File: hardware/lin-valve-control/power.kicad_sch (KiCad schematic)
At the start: 22 parts, among them U3 LTC3203BEDD-PBF, U4 BD9G341EFJ

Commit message: Uptdate title block
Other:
- company: (none) -> Gavin Hurlbut
- title: (none) -> LINBus Valve Controller
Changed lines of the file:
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@@
 (kicad_sch (version 20211123) (generator eeschema)
   (paper "A4")
+  (title_block
+    (title "LINBus Valve Controller")
+    (date "2023-02-17")
+    (rev "1.0")
+    (company "Gavin Hurlbut")
+  )
   (junction (at 109.347 133.096) (diameter 0) (color 0 0 0 0)
   )

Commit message: Add PCA9536 for the LINBus Address
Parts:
- renumbered U3 to U4, U4 to U5
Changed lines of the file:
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@@
   (symbol (lib_id "power:GND") (at 144.145 89.789 0) (unit 1)
     (in_bom yes) (on_board yes) (fields_autoplaced)
-    (property "Reference" "#PWR027" (id 0) (at 144.145 96.139 0)
+    (property "Reference" "#PWR030" (id 0) (at 144.145 96.139 0)
       (effects (font (size 1.27 1.27)) hide)
     )
@@
   (symbol (lib_id "power:+3V3") (at 100.457 116.967 0) (unit 1)
     (in_bom yes) (on_board yes) (fields_autoplaced)
-    (property "Reference" "#PWR021" (id 0) (at 100.457 120.777 0)
+    (property "Reference" "#PWR024" (id 0) (at 100.457 120.777 0)
       (effects (font (size 1.27 1.27)) hide)
     )
@@
   (symbol (lib_id "power:GND") (at 100.457 152.4 0) (unit 1)
     (in_bom yes) (on_board yes) (fields_autoplaced)
-    (property "Reference" "#PWR022" (id 0) (at 100.457 158.75 0)
+    (property "Reference" "#PWR025" (id 0) (at 100.457 158.75 0)
       (effects (font (size 1.27 1.27)) hide)
     )
@@
   (symbol (lib_id "power:GND") (at 197.358 58.674 0) (unit 1)
     (in_bom yes) (on_board yes) (fields_autoplaced)
-    (property "Reference" "#PWR033" (id 0) (at 197.358 65.024 0)
+    (property "Reference" "#PWR036" (id 0) (at 197.358 65.024 0)
       (effects (font (size 1.27 1.27)) hide)
     )
@@
   (symbol (lib_id "power:+3V3") (at 197.358 41.656 0) (unit 1)
     (in_bom yes) (on_board yes) (fields_autoplaced)
-    (property "Reference" "#PWR032" (id 0) (at 197.358 45.466 0)
+    (property "Reference" "#PWR035" (id 0) (at 197.358 45.466 0)
       (effects (font (size 1.27 1.27)) hide)
     )
@@
   (symbol (lib_id "power:GND") (at 149.098 56.515 0) (unit 1)
     (in_bom yes) (on_board yes) (fields_autoplaced)
-    (property "Reference" "#PWR028" (id 0) (at 149.098 62.865 0)
+    (property "Reference" "#PWR031" (id 0) (at 149.098 62.865 0)
       (effects (font (size 1.27 1.27)) hide)
     )
@@
   (symbol (lib_id "power:+BATT") (at 76.454 51.435 0) (unit 1)
     (in_bom yes) (on_board yes) (fields_autoplaced)
-    (property "Reference" "#PWR016" (id 0) (at 76.454 55.245 0)
+    (property "Reference" "#PWR019" (id 0) (at 76.454 55.245 0)
       (effects (font (size 1.27 1.27)) hide)
     )
@@
   (symbol (lib_id "Beirdo:BD9G341EFJ") (at 131.191 65.278 0) (unit 1)
     (in_bom yes) (on_board yes) (fields_autoplaced)
-    (property "Reference" "U4" (id 0) (at 133.2104 50.165 0)
+    (property "Reference" "U5" (id 0) (at 133.2104 50.165 0)
       (effects (font (size 1.27 1.27)) (justify left))
     )
@@
   (symbol (lib_id "power:GND") (at 89.027 150.114 0) (unit 1)
     (in_bom yes) (on_board yes) (fields_autoplaced)
-    (property "Reference" "#PWR018" (id 0) (at 89.027 156.464 0)
+    (property "Reference" "#PWR021" (id 0) (at 89.027 156.464 0)
       (effects (font (size 1.27 1.27)) hide)
     )
@@
   (symbol (lib_id "power:GND") (at 170.053 76.2 0) (unit 1)
     (in_bom yes) (on_board yes) (fields_autoplaced)
-    (property "Reference" "#PWR030" (id 0) (at 170.053 82.55 0)
+    (property "Reference" "#PWR033" (id 0) (at 170.053 82.55 0)
       (effects (font (size 1.27 1.27)) hide)
     )
@@
   (symbol (lib_id "power:+5V") (at 198.755 131.191 0) (unit 1)
     (in_bom yes) (on_board yes) (fields_autoplaced)
-    (property "Reference" "#PWR034" (id 0) (at 198.755 135.001 0)
+    (property "Reference" "#PWR037" (id 0) (at 198.755 135.001 0)
       (effects (font (size 1.27 1.27)) hide)
     )
@@
   (symbol (lib_id "power:GND") (at 111.887 156.21 0) (unit 1)
     (in_bom yes) (on_board yes) (fields_autoplaced)
-    (property "Reference" "#PWR024" (id 0) (at 111.887 162.56 0)
+    (property "Reference" "#PWR027" (id 0) (at 111.887 162.56 0)
       (effects (font (size 1.27 1.27)) hide)
     )
@@
   (symbol (lib_id "power:GND") (at 94.488 69.723 0) (unit 1)
     (in_bom yes) (on_board yes) (fields_autoplaced)
-    (property "Reference" "#PWR020" (id 0) (at 94.488 76.073 0)
+    (property "Reference" "#PWR023" (id 0) (at 94.488 76.073 0)
       (effects (font (size 1.27 1.27)) hide)
     )
@@
   (symbol (lib_id "power:GND") (at 198.755 145.669 0) (unit 1)
     (in_bom yes) (on_board yes) (fields_autoplaced)
-    (property "Reference" "#PWR035" (id 0) (at 198.755 152.019 0)
+    (property "Reference" "#PWR038" (id 0) (at 198.755 152.019 0)
       (effects (font (size 1.27 1.27)) hide)
     )
@@
   (symbol (lib_id "power:+3V3") (at 168.275 125.984 0) (unit 1)
     (in_bom yes) (on_board yes) (fields_autoplaced)
-    (property "Reference" "#PWR029" (id 0) (at 168.275 129.794 0)
+    (property "Reference" "#PWR032" (id 0) (at 168.275 129.794 0)
       (effects (font (size 1.27 1.27)) hide)
     )
@@
   (symbol (lib_id "power:GND") (at 111.633 77.089 0) (unit 1)
     (in_bom yes) (on_board yes) (fields_autoplaced)
-    (property "Reference" "#PWR023" (id 0) (at 111.633 83.439 0)
+    (property "Reference" "#PWR026" (id 0) (at 111.633 83.439 0)
       (effects (font (size 1.27 1.27)) hide)
     )
@@
   (symbol (lib_id "power:+12V") (at 94.488 52.705 0) (unit 1)
     (in_bom yes) (on_board yes) (fields_autoplaced)
-    (property "Reference" "#PWR019" (id 0) (at 94.488 56.515 0)
+    (property "Reference" "#PWR022" (id 0) (at 94.488 56.515 0)
       (effects (font (size 1.27 1.27)) hide)
     )
@@
   (symbol (lib_id "UltraLibrarian:LTC3203BEDD-PBF") (at 114.554 133.096 0) (unit 1)
     (in_bom yes) (on_board yes) (fields_autoplaced)
-    (property "Reference" "U3" (id 0) (at 139.954 122.682 0)
+    (property "Reference" "U4" (id 0) (at 139.954 122.682 0)
       (effects (font (size 1.524 1.524)))
     )
@@
   (symbol (lib_id "power:GND") (at 128.651 80.645 0) (unit 1)
     (in_bom yes) (on_board yes) (fields_autoplaced)
-    (property "Reference" "#PWR025" (id 0) (at 128.651 86.995 0)
+    (property "Reference" "#PWR028" (id 0) (at 128.651 86.995 0)
       (effects (font (size 1.27 1.27)) hide)
     )
@@
   (symbol (lib_id "power:GND") (at 179.705 58.928 0) (unit 1)
     (in_bom yes) (on_board yes) (fields_autoplaced)
-    (property "Reference" "#PWR031" (id 0) (at 179.705 65.278 0)
+    (property "Reference" "#PWR034" (id 0) (at 179.705 65.278 0)
       (effects (font (size 1.27 1.27)) hide)
     )
@@
   (symbol (lib_id "power:GND") (at 133.731 89.789 0) (unit 1)
     (in_bom yes) (on_board yes) (fields_autoplaced)
-    (property "Reference" "#PWR026" (id 0) (at 133.731 96.139 0)
+    (property "Reference" "#PWR029" (id 0) (at 133.731 96.139 0)
       (effects (font (size 1.27 1.27)) hide)
     )
@@
   (symbol (lib_id "power:+3V3") (at 89.027 128.27 0) (unit 1)
     (in_bom yes) (on_board yes) (fields_autoplaced)
-    (property "Reference" "#PWR017" (id 0) (at 89.027 132.08 0)
-      (effects (font (size 1.27 1.27)) hide)
-    )
+    (property "Reference" "#PWR020" (id 0) (at 89.027 132.08 0)
+      (effects (font (size 1.27 1.27)) hide)
+    )

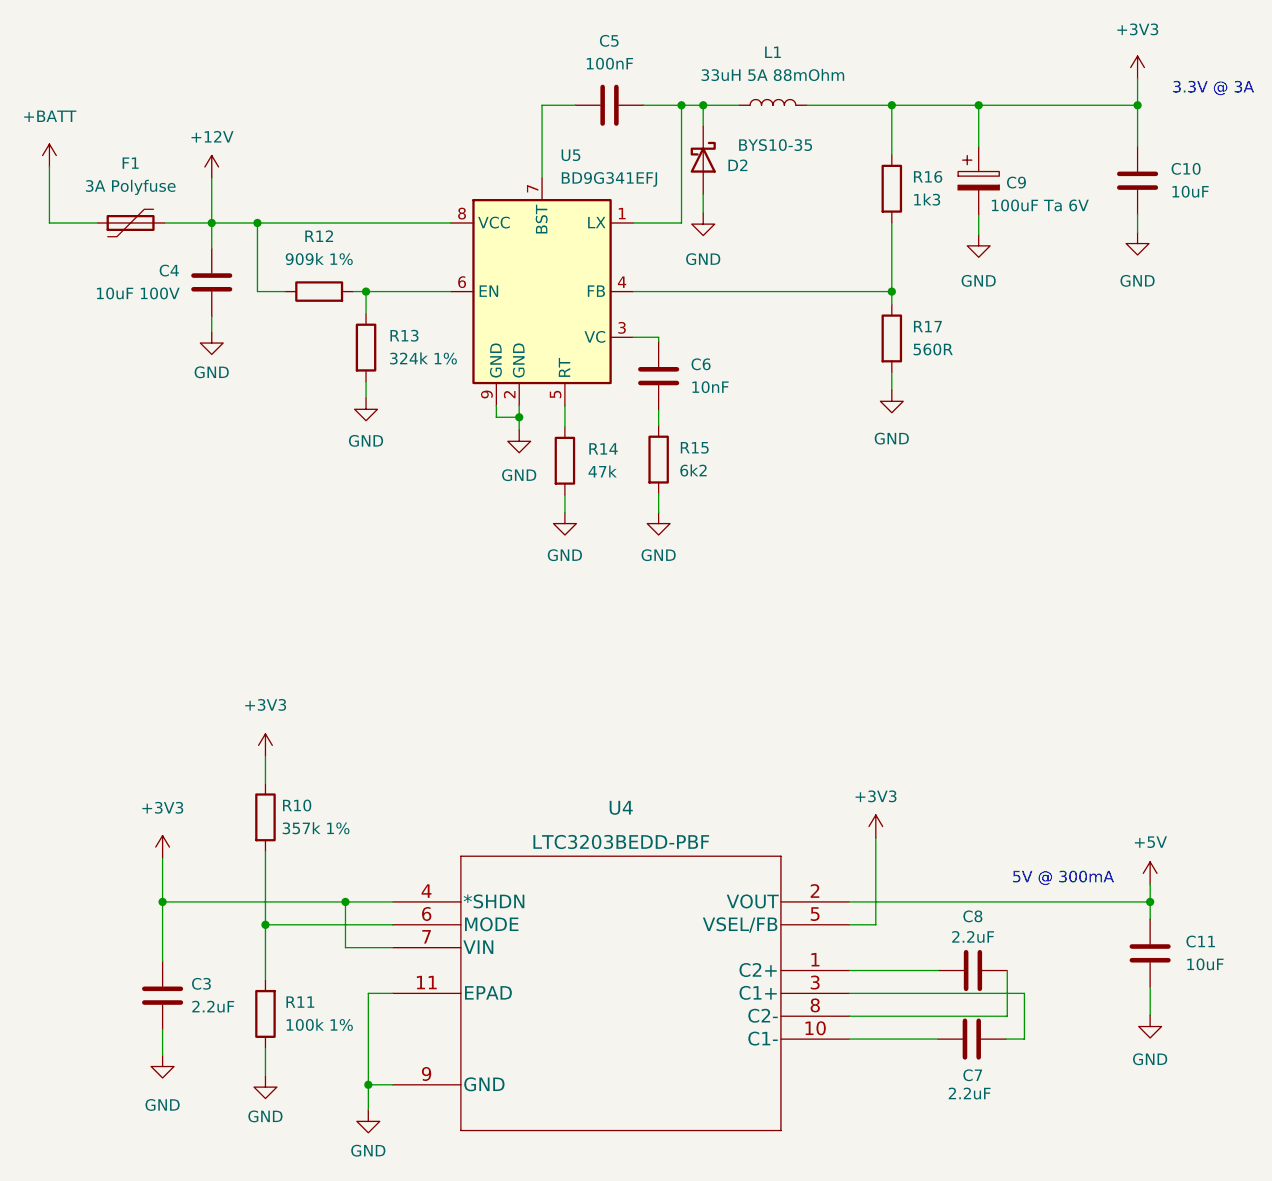
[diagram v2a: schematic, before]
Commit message: Rework valve-controller board, simplify firmware
- linbus_interface and linbus_registers moved to the common lib.
- reworked them all to compile again
- removing PCA9536 from all boards, adding the voltage reg. module
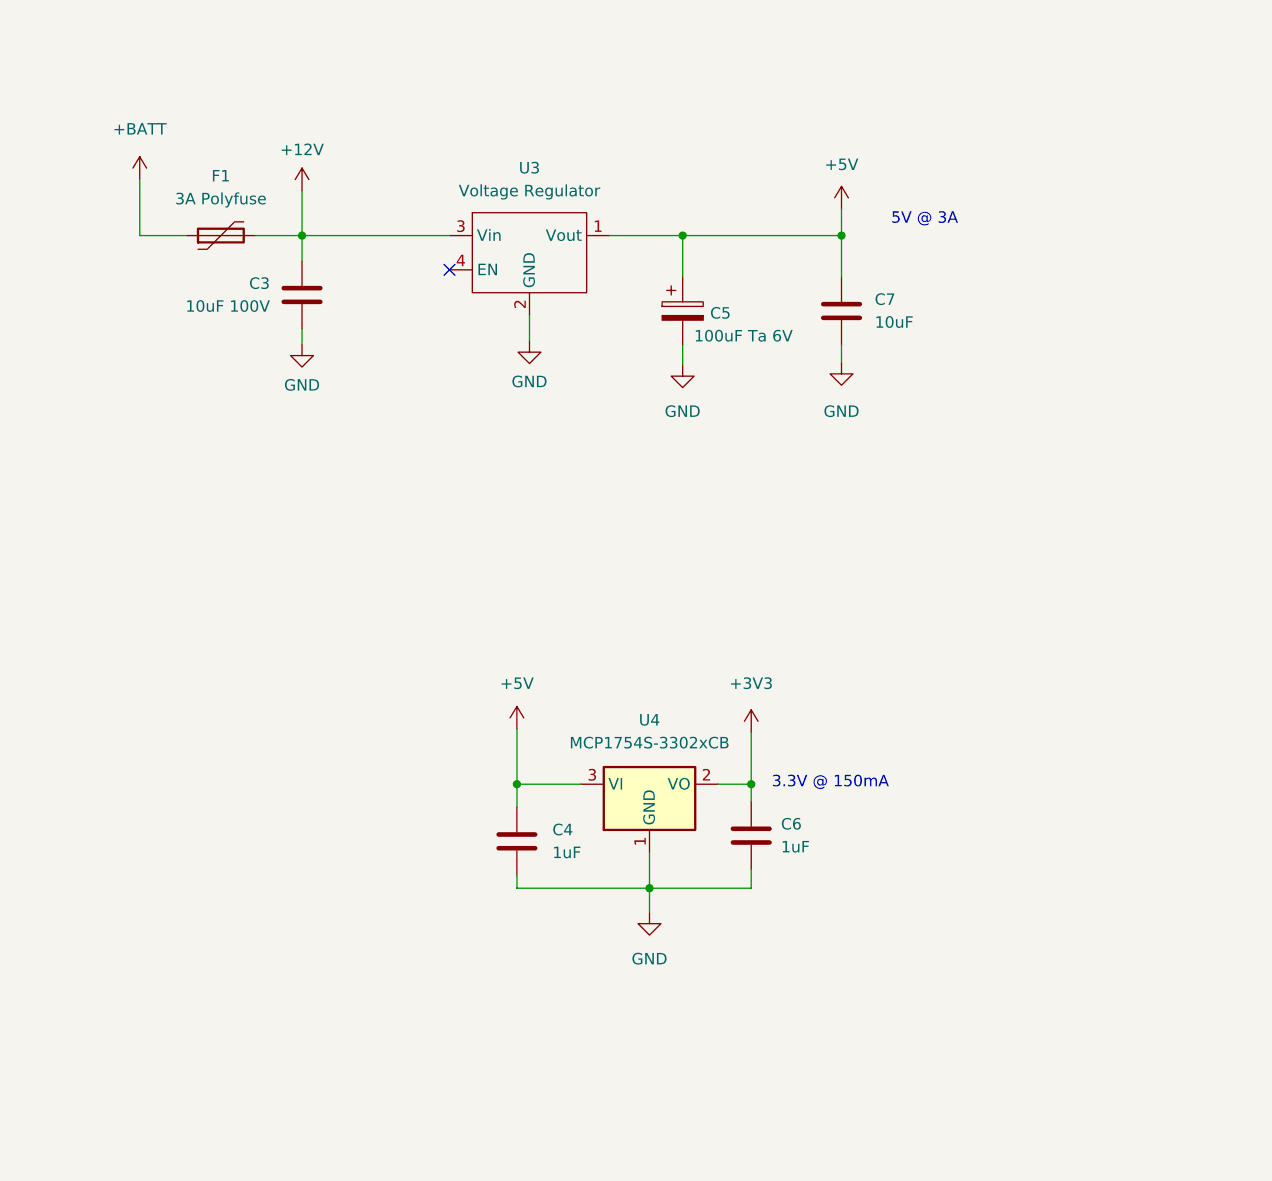
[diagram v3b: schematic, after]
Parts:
- removed C10, C11: 10uF, Capacitor_SMD:C_0805_2012Metric_Pad1.18x1.45mm_HandSolder, symbol Device:C
- removed C5: 100nF, Capacitor_SMD:C_0805_2012Metric_Pad1.18x1.45mm_HandSolder, symbol Device:C
- removed C8: 2.2uF, Capacitor_SMD:C_0805_2012Metric_Pad1.18x1.45mm_HandSolder, symbol Device:C
- removed C9: 100uF Ta 6V, Capacitor_Tantalum_SMD:CP_EIA-3216-10_Kemet-I_Pad1.58x1.35mm_HandSolder, symbol Device:C_Polarized
- removed D2: BYS10-35, Diode_SMD:D_SMA_Handsoldering, symbol Device:D_Schottky
- removed L1: 33uH 5A 88mOhm, Beirdo:PM4346.333NLT, symbol Device:L
- removed R10: 357k 1%, Resistor_SMD:R_0805_2012Metric_Pad1.20x1.40mm_HandSolder, symbol Device:R
- removed R11: 100k 1%, Resistor_SMD:R_0805_2012Metric_Pad1.20x1.40mm_HandSolder, symbol Device:R
- removed R12: 909k 1%, Resistor_SMD:R_0805_2012Metric_Pad1.20x1.40mm_HandSolder, symbol Device:R
- removed R13: 324k 1%, Resistor_SMD:R_0805_2012Metric_Pad1.20x1.40mm_HandSolder, symbol Device:R
- removed R14: 47k, Resistor_SMD:R_0805_2012Metric_Pad1.20x1.40mm_HandSolder, symbol Device:R
- removed R15: 6k2, Resistor_SMD:R_0805_2012Metric_Pad1.20x1.40mm_HandSolder, symbol Device:R
- removed R16: 1k3, Resistor_SMD:R_0805_2012Metric_Pad1.20x1.40mm_HandSolder, symbol Device:R
- removed R17: 560R, Resistor_SMD:R_0805_2012Metric_Pad1.20x1.40mm_HandSolder, symbol Device:R
- removed U4: LTC3203BEDD-PBF, UltraLibrarian:LTC3203BEDD-PBF, symbol UltraLibrarian:LTC3203BEDD-PBF
- removed U5: BD9G341EFJ, Package_SO:HTSOP-8-1EP_3.9x4.9mm_P1.27mm_EP2.4x3.2mm_ThermalVias, symbol Beirdo:BD9G341EFJ
- added C5: 100uF Ta 6V, Capacitor_Tantalum_SMD:CP_EIA-3216-10_Kemet-I_Pad1.58x1.35mm_HandSolder, symbol Device:C_Polarized
- added U3: Voltage Regulator, Beirdo:Switching_Regulator_Module, symbol Beirdo:Switching_Regulator_Module
- added U4: MCP1754S-3302xCB, Package_TO_SOT_SMD:SOT-23, symbol Regulator_Linear:MCP1754S-3302xCB
- C3: value 2.2uF -> 10uF 100V; footprint Capacitor_SMD:C_0805_2012Metric_Pad1.18x1.45mm_HandSolder -> Capacitor_SMD:C_1210_3225Metric_Pad1.33x2.70mm_HandSolder
- C4: value 10uF 100V -> 1uF; footprint Capacitor_SMD:C_1210_3225Metric_Pad1.33x2.70mm_HandSolder -> Capacitor_SMD:C_0805_2012Metric_Pad1.18x1.45mm_HandSolder
- C6: value 10nF -> 1uF
- C7: value 2.2uF -> 10uF
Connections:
- net +12V: now also C3.1, U3.3 (Vin); no longer C4.1
- net +3V3: now also C6.1, U4.2 (VO); no longer C3.1
- net +5V: now also C4.1, C7.1, C5.1, U3.1 (Vout), U4.3 (VI)
- net GND: now also C6.2, C7.2, C5.2, U3.2 (GND), U4.1 (GND)
- no-connect marks 0 -> 1
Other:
- note added: "3.3V @ 150mA"
- note added: "5V @ 3A"
- note removed: "3.3V @ 3A"
- note removed: "5V @ 300mA"
